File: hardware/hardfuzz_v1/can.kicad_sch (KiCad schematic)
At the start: 7 parts, among them J5 CAN, U9 SN65HVD230

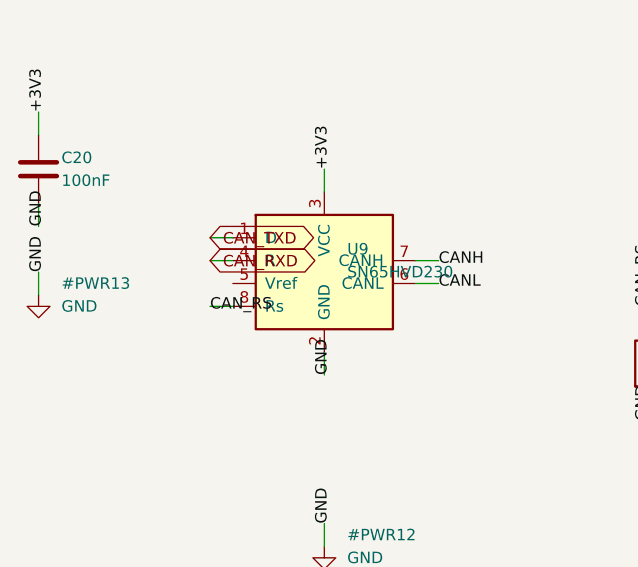
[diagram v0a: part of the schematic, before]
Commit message: hardware(kigen): review cleanup — NC flags, MPNs, PG/flag fixes, FPGA on A1
Address kicad-happy skill + ERC findings on the hierarchical board:
- no-connect flags on all intentional spare pins (unconnected 238 -> 0)
- MPNs on 16 ICs/connectors; grid-snapped endpoints
- fix buck PG mis-map (was tied to VIN) and drop double-driver PWR_FLAGs
- rename FT core rail VDDCORE_FT so PP-001 reads it as an internal rail (info)
- FPGA sub-sheet on A1 so all 5 units fit on the page
kigen gains no_connect + MPN emission. Skill review now: 1 error (SS-001
sourcing gate, needs passive MPNs) + benign info; netlist connectivity intact.

Co-Authored-By: Claude Opus 4.8 <noreply@anthropic.com>
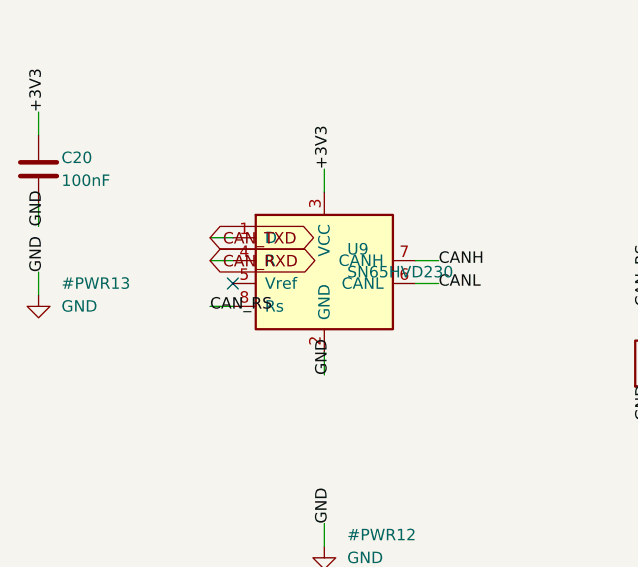
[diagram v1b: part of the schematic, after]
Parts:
- U9: MPN (none) -> SN65HVD230DR
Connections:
- no-connect marks 0 -> 1
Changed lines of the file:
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@@
 		(property "Footprint" "" (at 149.86 80.01 0)
+			(effects (font (size 1.27 1.27)) (hide yes)))
+		(property "MPN" "SN65HVD230DR" (at 149.86 80.01 0)
 			(effects (font (size 1.27 1.27)) (hide yes)))
 		(pin "1")
@@
 		(instances
 			(project "hardfuzz_v1"
-				(path "/d4330dca-89ae-4793-b016-d6c0afd5f7c5/7bbb6fde-0e0c-4ca5-9fe9-54ff7debdf15" (reference "U9") (unit 1))))
+				(path "/2a7cfa2e-8c6d-45dc-afe3-6b5c0cf25bc7/d23c023f-f11d-4da9-bd6e-47a3c47eae82" (reference "U9") (unit 1))))
 	)
 	(wire (pts (xy 139.70 77.47) (xy 137.16 77.47))
@@
 		(effects (font (size 1.27 1.27)) (justify left))
 )
+	(no_connect (at 139.70 82.55))
 	(symbol
 		(lib_id "power:+3V3")
@@
 		(instances
 			(project "hardfuzz_v1"
-				(path "/d4330dca-89ae-4793-b016-d6c0afd5f7c5/7bbb6fde-0e0c-4ca5-9fe9-54ff7debdf15" (reference "#PWR11") (unit 1))))
+				(path "/2a7cfa2e-8c6d-45dc-afe3-6b5c0cf25bc7/d23c023f-f11d-4da9-bd6e-47a3c47eae82" (reference "#PWR11") (unit 1))))
 	)
 	(wire (pts (xy 149.86 44.45) (xy 149.86 46.99))
@@
 		(instances
 			(project "hardfuzz_v1"
-				(path "/d4330dca-89ae-4793-b016-d6c0afd5f7c5/7bbb6fde-0e0c-4ca5-9fe9-54ff7debdf15" (reference "#PWR12") (unit 1))))
+				(path "/2a7cfa2e-8c6d-45dc-afe3-6b5c0cf25bc7/d23c023f-f11d-4da9-bd6e-47a3c47eae82" (reference "#PWR12") (unit 1))))
 	)
 	(wire (pts (xy 149.86 111.76) (xy 149.86 109.22))
@@
 		(instances
 			(project "hardfuzz_v1"
-				(path "/d4330dca-89ae-4793-b016-d6c0afd5f7c5/7bbb6fde-0e0c-4ca5-9fe9-54ff7debdf15" (reference "C20") (unit 1))))
+				(path "/2a7cfa2e-8c6d-45dc-afe3-6b5c0cf25bc7/d23c023f-f11d-4da9-bd6e-47a3c47eae82" (reference "C20") (unit 1))))
 	)
 	(wire (pts (xy 118.11 66.04) (xy 118.11 63.50))
@@
 		(instances
 			(project "hardfuzz_v1"
-				(path "/d4330dca-89ae-4793-b016-d6c0afd5f7c5/7bbb6fde-0e0c-4ca5-9fe9-54ff7debdf15" (reference "R20") (unit 1))))
+				(path "/2a7cfa2e-8c6d-45dc-afe3-6b5c0cf25bc7/d23c023f-f11d-4da9-bd6e-47a3c47eae82" (reference "R20") (unit 1))))
 	)
 	(wire (pts (xy 185.42 87.63) (xy 185.42 85.09))
@@
 		(instances
 			(project "hardfuzz_v1"
-				(path "/d4330dca-89ae-4793-b016-d6c0afd5f7c5/7bbb6fde-0e0c-4ca5-9fe9-54ff7debdf15" (reference "#PWR13") (unit 1))))
+				(path "/2a7cfa2e-8c6d-45dc-afe3-6b5c0cf25bc7/d23c023f-f11d-4da9-bd6e-47a3c47eae82" (reference "#PWR13") (unit 1))))
 	)
 	(wire (pts (xy 118.11 83.82) (xy 118.11 81.28))
@@
 		(instances
 			(project "hardfuzz_v1"
-				(path "/d4330dca-89ae-4793-b016-d6c0afd5f7c5/7bbb6fde-0e0c-4ca5-9fe9-54ff7debdf15" (reference "R21") (unit 1))))
+				(path "/2a7cfa2e-8c6d-45dc-afe3-6b5c0cf25bc7/d23c023f-f11d-4da9-bd6e-47a3c47eae82" (reference "R21") (unit 1))))
 	)
 	(wire (pts (xy 209.55 55.88) (xy 209.55 53.34))
@@
 		(instances
 			(project "hardfuzz_v1"
-				(path "/d4330dca-89ae-4793-b016-d6c0afd5f7c5/7bbb6fde-0e0c-4ca5-9fe9-54ff7debdf15" (reference "R22") (unit 1))))
+				(path "/2a7cfa2e-8c6d-45dc-afe3-6b5c0cf25bc7/d23c023f-f11d-4da9-bd6e-47a3c47eae82" (reference "R22") (unit 1))))
 	)
 	(wire (pts (xy 209.55 96.52) (xy 209.55 93.98))
@@
 		(instances
 			(project "hardfuzz_v1"
-				(path "/d4330dca-89ae-4793-b016-d6c0afd5f7c5/7bbb6fde-0e0c-4ca5-9fe9-54ff7debdf15" (reference "C21") (unit 1))))
+				(path "/2a7cfa2e-8c6d-45dc-afe3-6b5c0cf25bc7/d23c023f-f11d-4da9-bd6e-47a3c47eae82" (reference "C21") (unit 1))))
 	)
 	(wire (pts (xy 229.87 76.20) (xy 229.87 73.66))
@@
 		(instances
 			(project "hardfuzz_v1"
-				(path "/d4330dca-89ae-4793-b016-d6c0afd5f7c5/7bbb6fde-0e0c-4ca5-9fe9-54ff7debdf15" (reference "#PWR14") (unit 1))))
+				(path "/2a7cfa2e-8c6d-45dc-afe3-6b5c0cf25bc7/d23c023f-f11d-4da9-bd6e-47a3c47eae82" (reference "#PWR14") (unit 1))))
 	)
 	(wire (pts (xy 229.87 96.52) (xy 229.87 93.98))
@@
 		(instances
 			(project "hardfuzz_v1"
-				(path "/d4330dca-89ae-4793-b016-d6c0afd5f7c5/7bbb6fde-0e0c-4ca5-9fe9-54ff7debdf15" (reference "J5") (unit 1))))
+				(path "/2a7cfa2e-8c6d-45dc-afe3-6b5c0cf25bc7/d23c023f-f11d-4da9-bd6e-47a3c47eae82" (reference "J5") (unit 1))))
 	)
 	(wire (pts (xy 265.43 77.47) (xy 262.89 77.47))
@@
 )
 	(sheet_instances
-		(path "/7bbb6fde-0e0c-4ca5-9fe9-54ff7debdf15" (page "4")))
+		(path "/d23c023f-f11d-4da9-bd6e-47a3c47eae82" (page "4")))
 	(embedded_fonts no)
 )

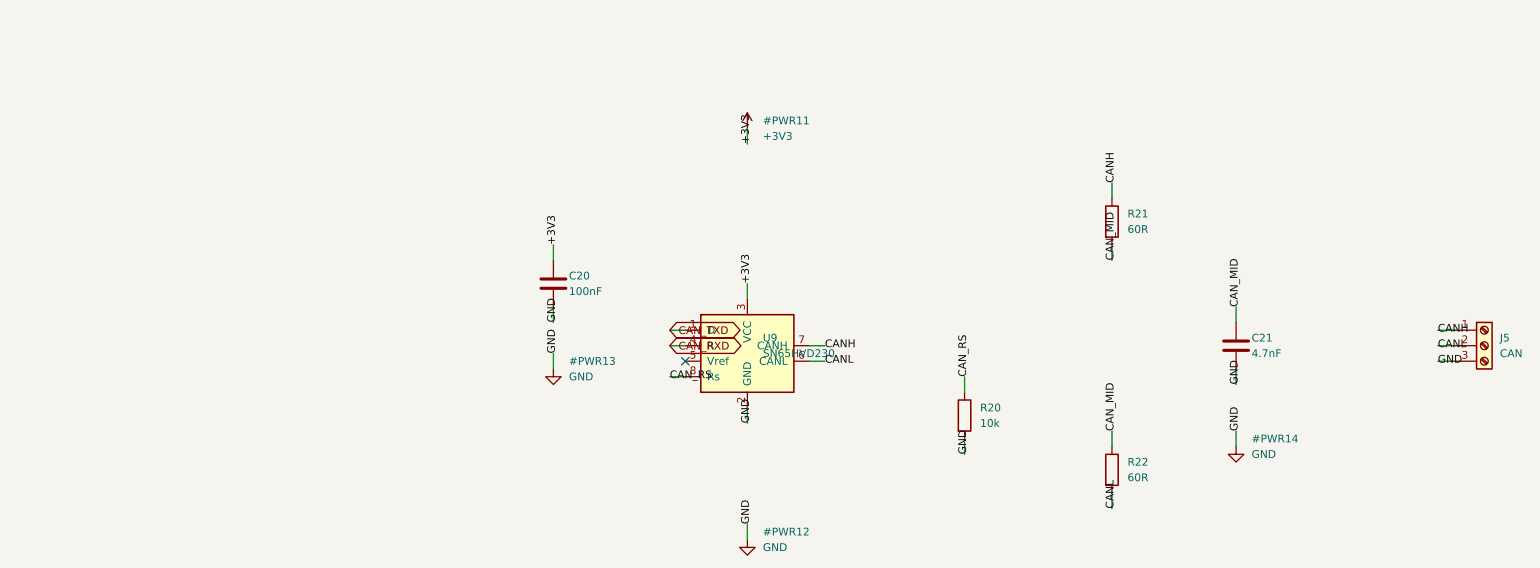
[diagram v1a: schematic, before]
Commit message: hardware(kigen): readability — auto-fit paper/margins + labels justified outward
Two fixes so every sheet reads cleanly:
- autofit(): translate each sheet's content inside a margin and pick the smallest
  standard paper that contains it (pins + labels + text) — nothing spills past the
  frame anymore (level-shift/USB previously exceeded A3).
- direction-aware label justification: net labels now extend AWAY from the
  component body (left-side pins' text goes left, right-side right, connector
  columns split) instead of overprinting the symbol.
Netlist connectivity + 0 collisions verified unchanged.

Co-Authored-By: Claude Opus 4.8 <noreply@anthropic.com>
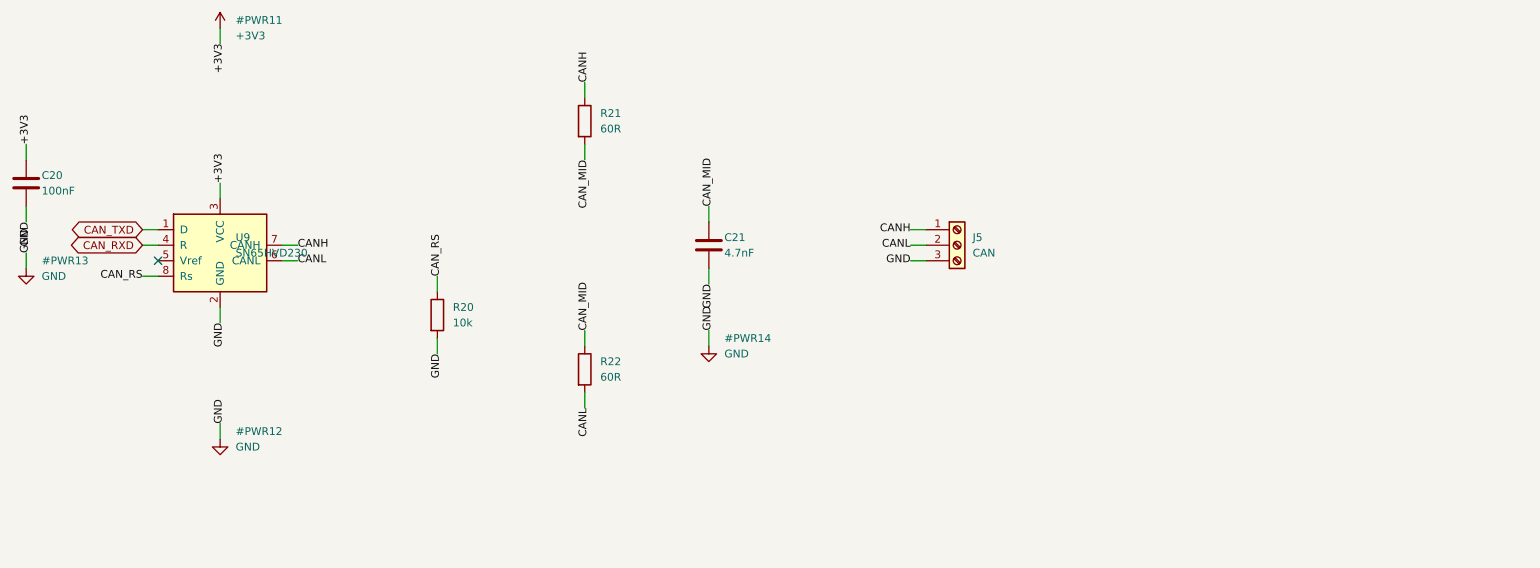
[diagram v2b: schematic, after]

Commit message: hardware: generate placed PCB (hardfuzz_v1.kicad_pcb) + footprints; rename root
kigen_pcb.py generates the PCB from the schematic netlist: loads each part's
stock .kicad_mod, shelf-packs footprints (origin-offset so courtyards don't
overlap), injects pad nets, and adds a board outline + 2-layer stackup. Loads in
pcbnew with 68 footprints and 302 nets on the right pads; the 317 'unconnected'
are the unrouted nets (routing is interactive/autorouter — the generator sets it
up, doesn't draw copper).

Also: assigned real footprints to the 6 ICs that lacked them and fixed 2 wrong
names (all now resolve, incl BGA-324 + QFN-64). Renamed the root schematic/PCB to
hardfuzz_v1.* so the project opens linked as hardfuzz_v1.kicad_pro.

Co-Authored-By: Claude Opus 4.8 <noreply@anthropic.com>
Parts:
- J5: footprint TerminalBlock_Phoenix:TerminalBlock_Phoenix_MPT-0,5-3-2.54_1x03 -> TerminalBlock_Phoenix:TerminalBlock_Phoenix_MPT-0,5-3-2.54_1x03_P2.54mm_Horizontal
- U9: footprint (none) -> Package_SO:SOIC-8_3.9x4.9mm_P1.27mm
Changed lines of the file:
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@@
 		(property "Value" "SN65HVD230" (at 66.09 64.83 0)
 			(effects (font (size 1.27 1.27)) (justify left)))
-		(property "Footprint" "" (at 63.55 63.56 0)
+		(property "Footprint" "Package_SO:SOIC-8_3.9x4.9mm_P1.27mm" (at 63.55 63.56 0)
 			(effects (font (size 1.27 1.27)) (hide yes)))
 		(property "MPN" "SN65HVD230DR" (at 63.55 63.56 0)
@@
 		(instances
 			(project "hardfuzz_v1"
-				(path "/ba6f588c-ef80-4b6d-a64b-de96b4dacc26/57be7944-ada4-4343-afc7-5b02feb0107c" (reference "U9") (unit 1))))
+				(path "/287a9ed2-a26a-4469-8d2c-da808579c5eb/2d6298ee-e122-45a2-9259-a01c7baa422a" (reference "U9") (unit 1))))
 	)
 	(wire (pts (xy 53.39 61.02) (xy 50.85 61.02))
@@
 		(instances
 			(project "hardfuzz_v1"
-				(path "/ba6f588c-ef80-4b6d-a64b-de96b4dacc26/57be7944-ada4-4343-afc7-5b02feb0107c" (reference "#PWR11") (unit 1))))
+				(path "/287a9ed2-a26a-4469-8d2c-da808579c5eb/2d6298ee-e122-45a2-9259-a01c7baa422a" (reference "#PWR11") (unit 1))))
 	)
 	(wire (pts (xy 63.55 28.00) (xy 63.55 30.54))
@@
 		(instances
 			(project "hardfuzz_v1"
-				(path "/ba6f588c-ef80-4b6d-a64b-de96b4dacc26/57be7944-ada4-4343-afc7-5b02feb0107c" (reference "#PWR12") (unit 1))))
+				(path "/287a9ed2-a26a-4469-8d2c-da808579c5eb/2d6298ee-e122-45a2-9259-a01c7baa422a" (reference "#PWR12") (unit 1))))
 	)
 	(wire (pts (xy 63.55 95.31) (xy 63.55 92.77))
@@
 		(instances
 			(project "hardfuzz_v1"
-				(path "/ba6f588c-ef80-4b6d-a64b-de96b4dacc26/57be7944-ada4-4343-afc7-5b02feb0107c" (reference "C20") (unit 1))))
+				(path "/287a9ed2-a26a-4469-8d2c-da808579c5eb/2d6298ee-e122-45a2-9259-a01c7baa422a" (reference "C20") (unit 1))))
 	)
 	(wire (pts (xy 31.80 49.59) (xy 31.80 47.05))
@@
 		(instances
 			(project "hardfuzz_v1"
-				(path "/ba6f588c-ef80-4b6d-a64b-de96b4dacc26/57be7944-ada4-4343-afc7-5b02feb0107c" (reference "R20") (unit 1))))
+				(path "/287a9ed2-a26a-4469-8d2c-da808579c5eb/2d6298ee-e122-45a2-9259-a01c7baa422a" (reference "R20") (unit 1))))
 	)
 	(wire (pts (xy 99.11 71.18) (xy 99.11 68.64))
@@
 		(instances
 			(project "hardfuzz_v1"
-				(path "/ba6f588c-ef80-4b6d-a64b-de96b4dacc26/57be7944-ada4-4343-afc7-5b02feb0107c" (reference "#PWR13") (unit 1))))
+				(path "/287a9ed2-a26a-4469-8d2c-da808579c5eb/2d6298ee-e122-45a2-9259-a01c7baa422a" (reference "#PWR13") (unit 1))))
 	)
 	(wire (pts (xy 31.80 67.37) (xy 31.80 64.83))
@@
 		(instances
 			(project "hardfuzz_v1"
-				(path "/ba6f588c-ef80-4b6d-a64b-de96b4dacc26/57be7944-ada4-4343-afc7-5b02feb0107c" (reference "R21") (unit 1))))
+				(path "/287a9ed2-a26a-4469-8d2c-da808579c5eb/2d6298ee-e122-45a2-9259-a01c7baa422a" (reference "R21") (unit 1))))
 	)
 	(wire (pts (xy 123.24 39.43) (xy 123.24 36.89))
@@
 		(instances
 			(project "hardfuzz_v1"
-				(path "/ba6f588c-ef80-4b6d-a64b-de96b4dacc26/57be7944-ada4-4343-afc7-5b02feb0107c" (reference "R22") (unit 1))))
+				(path "/287a9ed2-a26a-4469-8d2c-da808579c5eb/2d6298ee-e122-45a2-9259-a01c7baa422a" (reference "R22") (unit 1))))
 	)
 	(wire (pts (xy 123.24 80.07) (xy 123.24 77.53))
@@
 		(instances
 			(project "hardfuzz_v1"
-				(path "/ba6f588c-ef80-4b6d-a64b-de96b4dacc26/57be7944-ada4-4343-afc7-5b02feb0107c" (reference "C21") (unit 1))))
+				(path "/287a9ed2-a26a-4469-8d2c-da808579c5eb/2d6298ee-e122-45a2-9259-a01c7baa422a" (reference "C21") (unit 1))))
 	)
 	(wire (pts (xy 143.56 59.75) (xy 143.56 57.21))
@@
 		(instances
 			(project "hardfuzz_v1"
-				(path "/ba6f588c-ef80-4b6d-a64b-de96b4dacc26/57be7944-ada4-4343-afc7-5b02feb0107c" (reference "#PWR14") (unit 1))))
+				(path "/287a9ed2-a26a-4469-8d2c-da808579c5eb/2d6298ee-e122-45a2-9259-a01c7baa422a" (reference "#PWR14") (unit 1))))
 	)
 	(wire (pts (xy 143.56 80.07) (xy 143.56 77.53))
@@
 		(property "Value" "CAN" (at 186.74 64.83 0)
 			(effects (font (size 1.27 1.27)) (justify left)))
-		(property "Footprint" "TerminalBlock_Phoenix:TerminalBlock_Phoenix_MPT-0,5-3-2.54_1x03" (at 184.20 63.56 0)
+		(property "Footprint" "TerminalBlock_Phoenix:TerminalBlock_Phoenix_MPT-0,5-3-2.54_1x03_P2.54mm_Horizontal" (at 184.20 63.56 0)
 			(effects (font (size 1.27 1.27)) (hide yes)))
 		(pin "1")
@@
 		(instances
 			(project "hardfuzz_v1"
-				(path "/ba6f588c-ef80-4b6d-a64b-de96b4dacc26/57be7944-ada4-4343-afc7-5b02feb0107c" (reference "J5") (unit 1))))
+				(path "/287a9ed2-a26a-4469-8d2c-da808579c5eb/2d6298ee-e122-45a2-9259-a01c7baa422a" (reference "J5") (unit 1))))
 	)
 	(wire (pts (xy 179.12 61.02) (xy 176.58 61.02))
@@
 )
 	(sheet_instances
-		(path "/57be7944-ada4-4343-afc7-5b02feb0107c" (page "4")))
+		(path "/2d6298ee-e122-45a2-9259-a01c7baa422a" (page "4")))
 	(embedded_fonts no)
 )
